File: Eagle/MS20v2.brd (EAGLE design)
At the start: 56 x 100 mm, 62 parts, among them IC1 LM13700M, IC2 TL074D, T1 2N3906, T2 2N3906

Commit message: updated Pot designations/values
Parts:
- CVTRIM: value A100K -> B100K
- renumbered FREQENCY to FREQUENCY
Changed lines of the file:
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@@
 <attribute name="NAME" x="12.2498" y="17.4704" size="1.27" layer="21" rot="R270"/>
 </element>
-<element name="CVTRIM" library="pot" package="EVUF" value="A100K" x="7.5" y="44.5" smashed="yes">
+<element name="CVTRIM" library="pot" package="EVUF" value="B100K" x="7.5" y="44.5" smashed="yes">
 <attribute name="NAME" x="4.5" y="50.5" size="1.27" layer="25"/>
 <attribute name="POPULARITY" value="0" x="57.03" y="34.34" size="1.778" layer="27" display="off"/>
 <attribute name="VALUE" x="3" y="35" size="1.27" layer="27"/>
 </element>
-<element name="FREQENCY" library="pot" package="EVUF" value="B50K" x="13.5" y="93" smashed="yes">
+<element name="FREQUENCY" library="pot" package="EVUF" value="B50K" x="13.5" y="93" smashed="yes">
 <attribute name="NAME" x="15.5" y="89.5" size="1.27" layer="25"/>
 <attribute name="POPULARITY" value="0" x="50.33" y="82.84" size="1.778" layer="27" display="off"/>
@@
 </signal>
 <signal name="N$40">
-<contactref element="FREQENCY" pad="2"/>
+<contactref element="FREQUENCY" pad="2"/>
 <contactref element="R25" pad="2"/>
 <wire x1="13.5" y1="86" x2="12" y2="87.5" width="0.254" layer="1"/>
@@
 </signal>
 <signal name="P-V">
-<contactref element="FREQENCY" pad="1"/>
+<contactref element="FREQUENCY" pad="1"/>
 <contactref element="J1" pad="3"/>
 <wire x1="11" y1="86" x2="12.23" y2="84.77" width="0.254" layer="1"/>
@@
 </signal>
 <signal name="P+V">
-<contactref element="FREQENCY" pad="3"/>
+<contactref element="FREQUENCY" pad="3"/>
 <contactref element="J1" pad="5"/>
 <wire x1="17.31" y1="82" x2="16" y2="83.31" width="0.254" layer="1"/>

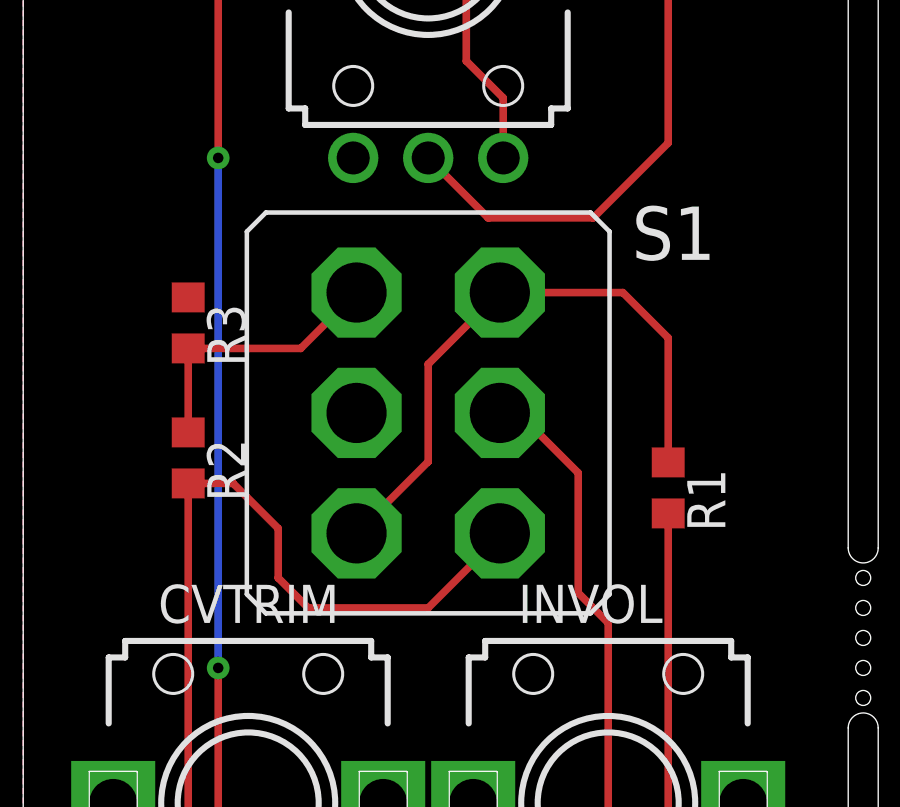
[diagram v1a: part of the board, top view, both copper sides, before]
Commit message: changed HP/LP switch type to  TL46 P0
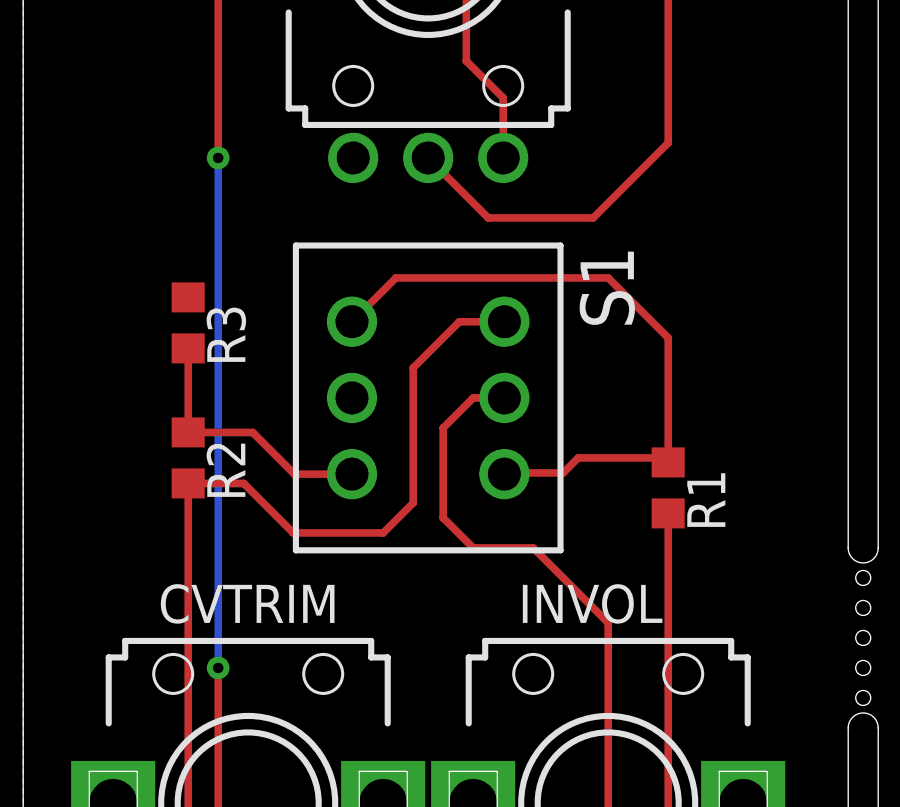
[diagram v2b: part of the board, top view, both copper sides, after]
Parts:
- S1: value DPDT 4.75mm -> TL46PO; device switch:320-938 -> switch:TL4XPO
- moved S1 0.50 mm to (13.5, 58.0), turned to 270 degrees
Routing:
- net N$30: track 21.9 -> 25.4 mm
- net PS2: track 72.2 -> 74.9 mm
- net N$3: track 20.4 -> 21.8 mm
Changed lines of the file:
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@@
 <attribute name="VALUE" x="54.284" y="91.9" size="0.4064" layer="27" rot="R90"/>
 </element>
-<element name="S1" library="switch" library_urn="urn:adsk.eagle:library:380" package="320-938" package3d_urn="urn:adsk.eagle:package:27685/1" value="DPDT 4.75mm" x="13.5" y="57.5" smashed="yes" rot="R180">
-<attribute name="NAME" x="23.08" y="64.38" size="1.778" layer="25" ratio="10" rot="R180"/>
-<attribute name="POPULARITY" value="1" x="13.5" y="57.5" size="1.778" layer="27" rot="R180" display="off"/>
-<attribute name="VALUE" x="18.58" y="67.025" size="1.778" layer="27" ratio="10" rot="R180"/>
+<element name="S1" library="switch" library_urn="urn:adsk.eagle:library:380" package="TL4XPO" package3d_urn="urn:adsk.eagle:package:27746/1" value="TL46PO" x="13.5" y="58" smashed="yes" rot="R270">
+<attribute name="NAME" x="18.58" y="63.08" size="1.778" layer="25" rot="R270"/>
+<attribute name="POPULARITY" value="1" x="13.5" y="58" size="1.778" layer="27" rot="R270" display="off"/>
+<attribute name="VALUE" x="7.15" y="63.08" size="1.778" layer="27" rot="R270"/>
 </element>
 </elements>
@@
 <vertex x="0" y="0"/>
 </polygon>
+<contactref element="IC2" pad="10"/>
 <contactref element="S1" pad="5"/>
-<contactref element="IC2" pad="10"/>
 <wire x1="19.5" y1="19.5" x2="35.5" y2="11.175" width="0" layer="19" extent="16-16"/>
 </signal>
 <signal name="N$3">
 <contactref element="R1" pad="1"/>
+<wire x1="21.5" y1="60" x2="21.5" y2="56" width="0.254" layer="1"/>
 <contactref element="S1" pad="4"/>
 <contactref element="S1" pad="3"/>
-<wire x1="21.5" y1="55.85" x2="21.5" y2="60" width="0.254" layer="1"/>
-<wire x1="21.5" y1="60" x2="19.9868" y2="61.5132" width="0.254" layer="1"/>
-<wire x1="19.9868" y1="61.5132" x2="15.8876" y2="61.5132" width="0.254" layer="1"/>
-<wire x1="11.1124" y1="53.4868" x2="13.5" y2="55.8744" width="0.254" layer="1"/>
-<wire x1="13.5" y1="59.1256" x2="15.8876" y2="61.5132" width="0.254" layer="1"/>
-<wire x1="13.5" y1="55.8744" x2="13.5" y2="59.1256" width="0.254" layer="1"/>
+<wire x1="21.5" y1="56" x2="21.5" y2="55.85" width="0.254" layer="1"/>
+<wire x1="10.96" y1="60.54" x2="12.42" y2="62" width="0.254" layer="1"/>
+<wire x1="12.42" y1="62" x2="19.5" y2="62" width="0.254" layer="1"/>
+<wire x1="19.5" y1="62" x2="21.5" y2="60" width="0.254" layer="1"/>
+<wire x1="16.04" y1="55.46" x2="16.08" y2="55.5" width="0.254" layer="1"/>
+<wire x1="18" y1="55.5" x2="18.5" y2="56" width="0.254" layer="1"/>
+<wire x1="18.5" y1="56" x2="21.5" y2="56" width="0.254" layer="1"/>
+<wire x1="16.08" y1="55.5" x2="18" y2="55.5" width="0.254" layer="1"/>
 </signal>
 <signal name="N$4">
@@
 <wire x1="5.5" y1="59.65" x2="5.5" y2="56.85" width="0.254" layer="1"/>
 <contactref element="S1" pad="6"/>
-<wire x1="5.5" y1="59.65" x2="9.2492" y2="59.65" width="0.254" layer="1"/>
-<wire x1="9.2492" y1="59.65" x2="11.1124" y2="61.5132" width="0.254" layer="1"/>
+<wire x1="5.5" y1="56.85" x2="7.65" y2="56.85" width="0.254" layer="1"/>
+<wire x1="9.04" y1="55.46" x2="10.96" y2="55.46" width="0.254" layer="1"/>
+<wire x1="7.65" y1="56.85" x2="9.04" y2="55.46" width="0.254" layer="1"/>
 </signal>
 <signal name="N$7">
@@
 <wire x1="19.5" y1="37.5" x2="19.5" y2="50.5" width="0.254" layer="1"/>
 <contactref element="S1" pad="2"/>
-<wire x1="18.5" y1="51.5" x2="18.5" y2="55.5" width="0.254" layer="1"/>
-<wire x1="18.5" y1="55.5" x2="16.5" y2="57.5" width="0.254" layer="1"/>
-<wire x1="16.5" y1="57.5" x2="15.8876" y2="57.5" width="0.254" layer="1"/>
-<wire x1="19.5" y1="50.5" x2="18.5" y2="51.5" width="0.254" layer="1"/>
+<wire x1="17" y1="53" x2="15" y2="53" width="0.254" layer="1"/>
+<wire x1="15" y1="53" x2="14" y2="54" width="0.254" layer="1"/>
+<wire x1="14" y1="54" x2="14" y2="57" width="0.254" layer="1"/>
+<wire x1="14" y1="57" x2="15" y2="58" width="0.254" layer="1"/>
+<wire x1="15" y1="58" x2="16.04" y2="58" width="0.254" layer="1"/>
+<wire x1="19.5" y1="50.5" x2="17" y2="53" width="0.254" layer="1"/>
 </signal>
 <signal name="N$31">
@@
 <wire x1="5.5" y1="42.5" x2="5.5" y2="55.15" width="0.254" layer="1"/>
 <contactref element="S1" pad="1"/>
-<wire x1="8.5" y1="53.65" x2="7" y2="55.15" width="0.254" layer="1"/>
-<wire x1="5.5" y1="55.15" x2="7" y2="55.15" width="0.254" layer="1"/>
-<wire x1="8.5" y1="53.65" x2="8.5" y2="52" width="0.254" layer="1"/>
-<wire x1="8.5" y1="52" x2="9.5" y2="51" width="0.254" layer="1"/>
-<wire x1="13.5" y1="51" x2="15.8876" y2="53.3876" width="0.254" layer="1"/>
-<wire x1="15.8876" y1="53.3876" x2="15.8876" y2="53.4868" width="0.254" layer="1"/>
-<wire x1="9.5" y1="51" x2="13.5" y2="51" width="0.254" layer="1"/>
+<wire x1="7.35" y1="55.15" x2="9" y2="53.5" width="0.254" layer="1"/>
+<wire x1="9" y1="53.5" x2="12" y2="53.5" width="0.254" layer="1"/>
+<wire x1="12" y1="53.5" x2="13" y2="54.5" width="0.254" layer="1"/>
+<wire x1="14.54" y1="60.54" x2="16.04" y2="60.54" width="0.254" layer="1"/>
+<wire x1="5.5" y1="55.15" x2="7.35" y2="55.15" width="0.254" layer="1"/>
+<wire x1="13" y1="54.5" x2="13" y2="59" width="0.254" layer="1"/>
+<wire x1="13" y1="59" x2="14.54" y2="60.54" width="0.254" layer="1"/>
 </signal>
 <signal name="N$5">
@@
 <wire x1="32.5" y1="72.5" x2="34.15" y2="72.5" width="0.254" layer="1"/>
 </signal>
+<signal name="N$24">
+</signal>
 </signals>

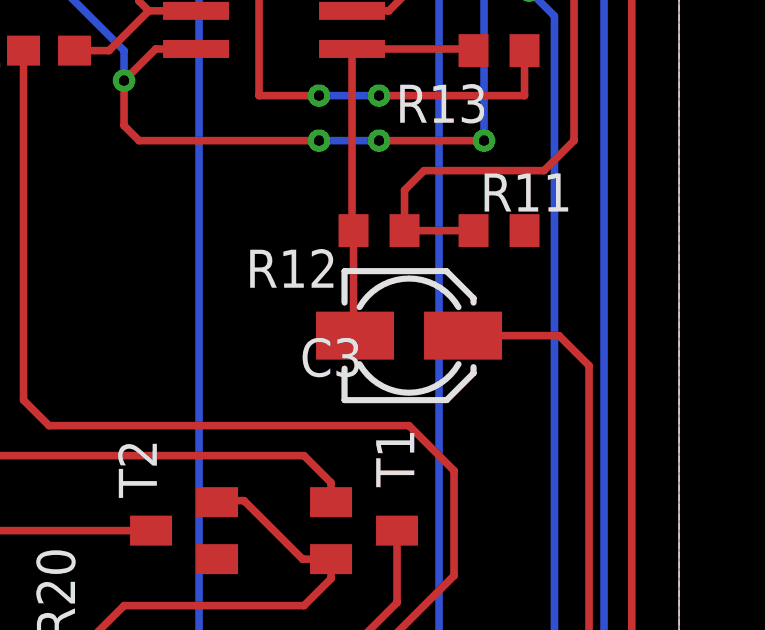
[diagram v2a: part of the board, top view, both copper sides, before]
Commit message: Changed 10uf cap to 0,47uf cap
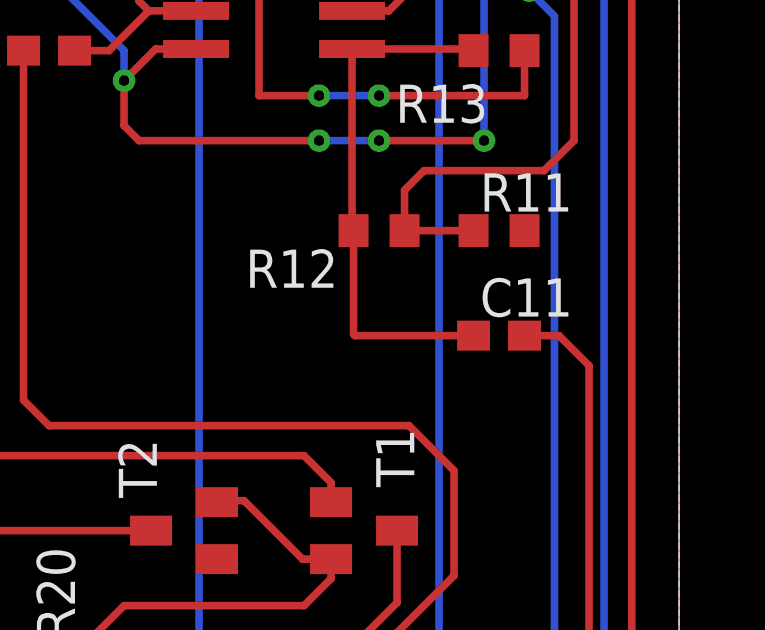
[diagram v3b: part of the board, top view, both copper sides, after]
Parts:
- removed C3: 10uf, rcl:153CLV-0405
- added C11: 0.47uF, rcl:C0603
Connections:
- net BQR: now also C11.2; no longer C3.+
- net N$16: now also C11.1; no longer C3.-
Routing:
- net N$16: track 13.7 -> 17.6 mm
- net BQR: track 78.1 -> 76.0 mm
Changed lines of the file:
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@@
 <attribute name="VALUE" x="44.865" y="86.095" size="1.27" layer="27"/>
-</element>
-<element name="C3" library="rcl" library_urn="urn:adsk.eagle:library:334" package="153CLV-0405" package3d_urn="urn:adsk.eagle:package:23397/2" value="10uf" x="47" y="52.5" smashed="yes">
-<attribute name="NAME" x="43.365" y="51.135" size="1.27" layer="25"/>
-<attribute name="POPULARITY" value="0" x="78.75" y="-17.35" size="1.778" layer="27" display="off"/>
-<attribute name="SPICEPREFIX" value="C" x="78.75" y="-17.35" size="1.778" layer="27" display="off"/>
-<attribute name="VALUE" x="41.865" y="52.595" size="1.27" layer="27"/>
 </element>
 <element name="C4" library="rcl" package="C0603" value="1nF" x="35" y="62" smashed="yes">
@@
 <attribute name="POPULARITY" value="1" x="13.5" y="58" size="1.778" layer="27" rot="R270" display="off"/>
 <attribute name="VALUE" x="7.15" y="63.08" size="1.778" layer="27" rot="R270"/>
+</element>
+<element name="C11" library="rcl" package="C0603" value="0.47uF" x="50" y="52.5" smashed="yes">
+<attribute name="NAME" x="49.365" y="53.135" size="1.27" layer="25"/>
+<attribute name="POPULARITY" value="73" x="50" y="52.5" size="1.778" layer="27" display="off"/>
+<attribute name="SPICEPREFIX" value="C" x="50" y="52.5" size="1.778" layer="27" display="off"/>
+<attribute name="VALUE" x="49.365" y="50.595" size="1.27" layer="27"/>
 </element>
 </elements>
@@
 <wire x1="45.1" y1="62.055" x2="45.1" y2="56.05" width="0.254" layer="1"/>
 <wire x1="45.1" y1="56.05" x2="45.15" y2="56" width="0.254" layer="1"/>
-<contactref element="C3" pad="-"/>
-<wire x1="45.15" y1="56" x2="45.15" y2="52.55" width="0.254" layer="1"/>
-<wire x1="45.15" y1="52.55" x2="45.2" y2="52.5" width="0.254" layer="1"/>
+<wire x1="45.15" y1="52.55" x2="45.15" y2="56" width="0.254" layer="1"/>
+<contactref element="C11" pad="1"/>
+<wire x1="49.15" y1="52.5" x2="45.2" y2="52.5" width="0.254" layer="1"/>
+<wire x1="45.2" y1="52.5" x2="45.15" y2="52.55" width="0.254" layer="1"/>
 </signal>
 <signal name="N$17">
@@
 <wire x1="45.5" y1="75.5" x2="43.77" y2="77.23" width="0.254" layer="16"/>
 <wire x1="43.77" y1="77.23" x2="43.77" y2="82" width="0.254" layer="16"/>
-<wire x1="52" y1="52.5" x2="53" y2="51.5" width="0.254" layer="1"/>
+<wire x1="53" y1="51.5" x2="52" y2="52.5" width="0.254" layer="1"/>
 <wire x1="51.5" y1="35" x2="47.5" y2="35" width="0.254" layer="1"/>
 <wire x1="53" y1="51.5" x2="53" y2="36.5" width="0.254" layer="1"/>
 <wire x1="53" y1="36.5" x2="51.5" y2="35" width="0.254" layer="1"/>
-<contactref element="C3" pad="+"/>
-<wire x1="48.8" y1="52.5" x2="52" y2="52.5" width="0.254" layer="1"/>
+<contactref element="C11" pad="2"/>
+<wire x1="52" y1="52.5" x2="50.85" y2="52.5" width="0.254" layer="1"/>
 </signal>
 <signal name="BCVIN">
